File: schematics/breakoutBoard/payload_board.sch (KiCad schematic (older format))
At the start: 5 parts, among them P1 CONN_02X50, P2 CONN_02X50, P3 CONN_02X50, P4 CONN_02X50

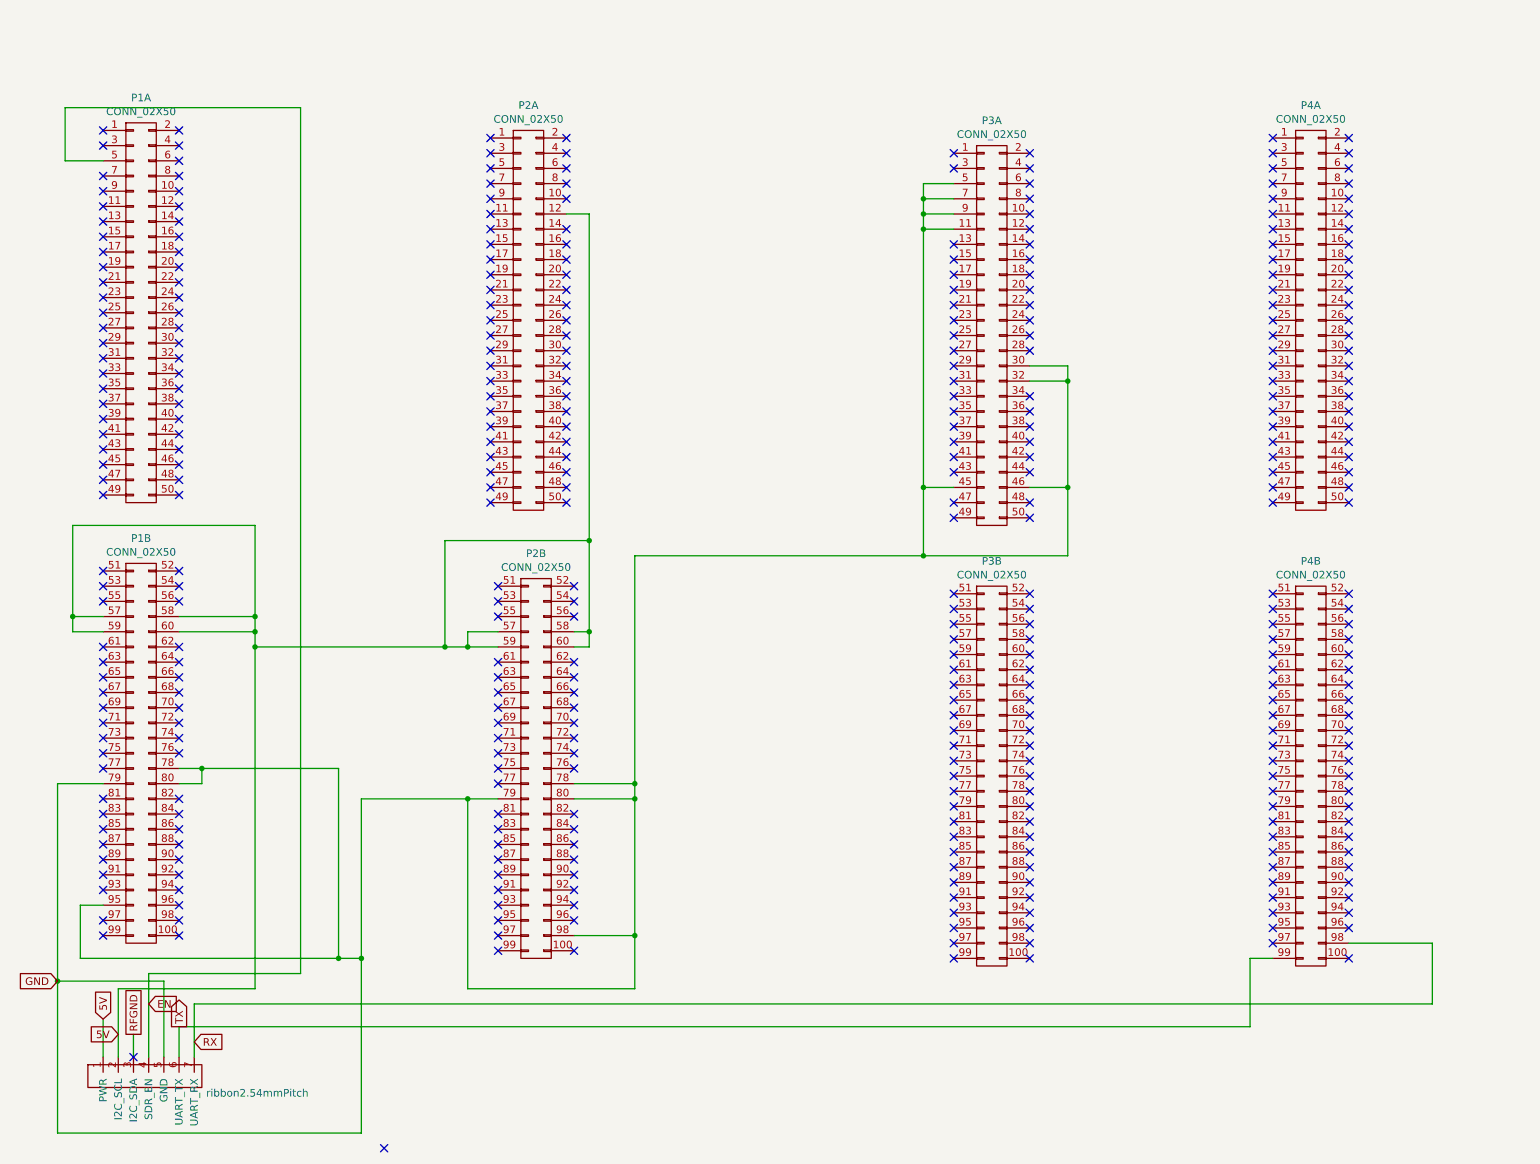
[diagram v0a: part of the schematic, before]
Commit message: Updated schematic
Cleaned up wires and re-did labels. Added additional grounds and verified pwr, TX and RX. Reference to Issues #1, #2, #3 and #5.
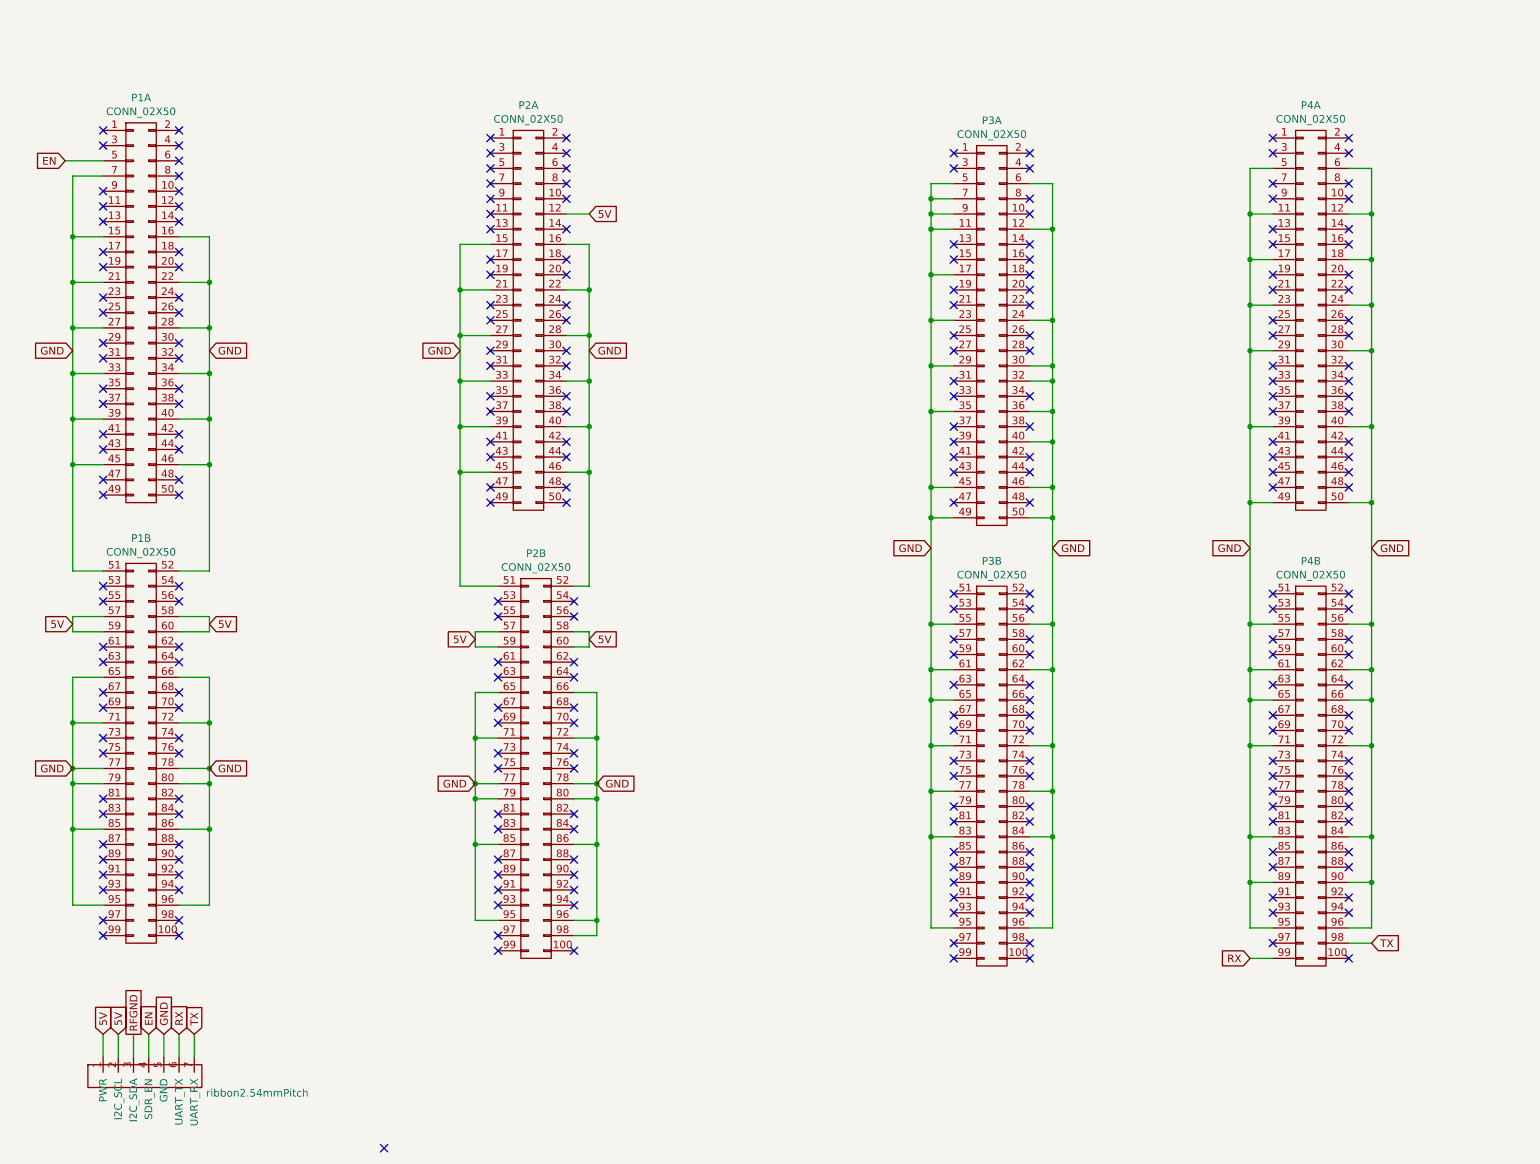
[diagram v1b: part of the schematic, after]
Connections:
- net GND: now also P1.15 (P15), P1.16 (P16), P1.21 (P21), P1.22 (P22), P1.27 (P27), P1.28 (P28), P1.33 (P33), P1.34 (P34), P1.39 (P39), P1.40 (P40), P1.45 (P45), P1.46 (P46), P1.51 (P51), P1.52 (P52), P1.65 (P65), P1.66 (P66), P1.7 (P7), P1.71 (P71), P1.72 (P72), P1.77 (P77), P1.85 (P85), P1.86 (P86), P1.96 (P96), P2.15 (P15), P2.16 (P16), P2.21 (P21), P2.22 (P22), P2.27 (P27), P2.28 (P28), P2.33 (P33), P2.34 (P34), P2.39 (P39), P2.40 (P40), P2.45 (P45), P2.46 (P46), P2.51 (P51), P2.52 (P52), P2.65 (P65), P2.66 (P66), P2.71 (P71), P2.72 (P72), P2.77 (P77), P2.85 (P85), P2.86 (P86), P2.95 (P95), P2.96 (P96), P3.12 (P12), P3.17 (P17), P3.23 (P23), P3.24 (P24), P3.29 (P29), P3.35 (P35), P3.36 (P36), P3.40 (P40), P3.49 (P49), P3.50 (P50), P3.55 (P55), P3.56 (P56), P3.6 (P6), P3.61 (P61), P3.62 (P62), P3.65 (P65), P3.71 (P71), P3.72 (P72), P3.77 (P77), P3.78 (P78), P3.83 (P83), P3.84 (P84), P3.95 (P95), P3.96 (P96), P4.11 (P11), P4.12 (P12), P4.17 (P17), P4.18 (P18), P4.23 (P23), P4.24 (P24), P4.29 (P29), P4.30 (P30), P4.39 (P39), P4.40 (P40), P4.49 (P49), P4.5 (P5), P4.50 (P50), P4.55 (P55), P4.56 (P56), P4.6 (P6), P4.61 (P61), P4.62 (P62), P4.65 (P65), P4.66 (P66), P4.71 (P71), P4.72 (P72), P4.83 (P83), P4.84 (P84), P4.89 (P89), P4.90 (P90), P4.95 (P95), P4.96 (P96)
- net RX: now also P4.99 (P99), e1.6 (UART_TX); no longer P4.98 (P98), e1.7 (UART_RX)
- net TX: now also P4.98 (P98), e1.7 (UART_RX); no longer P4.99 (P99), e1.6 (UART_TX)
- no-connect marks 374 -> 275

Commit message: Move files from main repo
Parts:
- removed e1: ribbon2.54mmPitch, Connector_PinHeader_2.54mm:PinHeader_1x07_P2.54mm_Vertical, symbol payload_board-rescue:ribbon2.54mmPitch
- added H1, H2, H3, H4, H5, H6, H7: MountingHole_Pad, MountingHole:MountingHole_2.2mm_M2_Pad, symbol Mechanical:MountingHole_Pad
- added J1: Conn_01x10, Connector_PinHeader_2.54mm:PinHeader_1x10_P2.54mm_Vertical, symbol Connector_Generic:Conn_01x10
- added SMA1, SMA2: Molex-MMCX-SMD, Mounting_Holes:Molex MMCX SMD 50Ohm, symbol payload_board-rescue:Molex-MMCX-SMD
- P1, P2, P3, P4: footprint breakoutBoard:BERGSTAK_100_PIN1_RIGHT -> 61083-101400LF:FCI_61083-101400LF
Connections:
- net GND: now also J1.10 (Pin_10); no longer P1.15 (P15), P1.16 (P16), P1.21 (P21), P1.22 (P22), P1.27 (P27), P1.28 (P28), P1.33 (P33), P1.34 (P34), P1.39 (P39), P1.40 (P40), P1.45 (P45), P1.46 (P46), P1.51 (P51), P1.52 (P52), P1.65 (P65), P1.66 (P66), P1.7 (P7), P1.71 (P71), P1.72 (P72), P1.77 (P77), P1.78 (P78), P1.79 (P79), P1.80 (P80), P1.85 (P85), P1.86 (P86), P1.95 (P95), P1.96 (P96), P2.15 (P15), P2.16 (P16), P2.21 (P21), P2.22 (P22), P2.27 (P27), P2.28 (P28), P2.33 (P33), P2.34 (P34), P2.39 (P39), P2.40 (P40), P2.45 (P45), P2.46 (P46), P2.51 (P51), P2.52 (P52), P2.65 (P65), P2.66 (P66), P2.71 (P71), P2.72 (P72), P2.77 (P77), P2.85 (P85), P2.86 (P86), P2.95 (P95), P2.96 (P96), P2.98 (P98), P3.12 (P12), P3.17 (P17), P3.23 (P23), P3.24 (P24), P3.29 (P29), P3.35 (P35), P3.36 (P36), P3.40 (P40), P3.45 (P45), P3.46 (P46), P3.49 (P49), P3.50 (P50), P3.55 (P55), P3.56 (P56), P3.6 (P6), P3.61 (P61), P3.62 (P62), P3.65 (P65), P3.71 (P71), P3.72 (P72), P3.77 (P77), P3.78 (P78), P3.83 (P83), P3.84 (P84), P3.95 (P95), P3.96 (P96), P4.11 (P11), P4.12 (P12), P4.17 (P17), P4.18 (P18), P4.23 (P23), P4.24 (P24), P4.29 (P29), P4.30 (P30), P4.39 (P39), P4.40 (P40), P4.49 (P49), P4.5 (P5), P4.50 (P50), P4.55 (P55), P4.56 (P56), P4.6 (P6), P4.61 (P61), P4.62 (P62), P4.65 (P65), P4.66 (P66), P4.71 (P71), P4.72 (P72), P4.83 (P83), P4.84 (P84), P4.89 (P89), P4.90 (P90), P4.95 (P95), P4.96 (P96)
- net SDA1: now reaches P2.13 (P13)
- net SDA1: now also H5.1, J1.7 (Pin_7)
- net SCL1: now reaches P2.14 (P14)
- net SCL1: now also H6.1, J1.8 (Pin_8)
- net SCL0: now reaches P2.17 (P17)
- net SCL0: now also H4.1, J1.6 (Pin_6)
- net SDA0: now reaches P2.19 (P19)
- net SDA0: now also H3.1, J1.5 (Pin_5)
- net ENABLE: now reaches P2.5 (P5)
- net ENABLE: now also H7.1, J1.9 (Pin_9)
- net UART_TX: now reaches P4.14 (P14)
- net UART_TX: now also H2.1, J1.4 (Pin_4)
- net UART_RX: now reaches P4.16 (P16)
- net UART_RX: now also H1.1, J1.3 (Pin_3)
- net 5V renamed 5v
- net 5v: now also J1.1 (Pin_1)
- net EN: no longer names the net of P1.5 (P5)
- net RX: no longer names the net of P4.99 (P99)
- net TX: no longer names the net of P4.98 (P98)
- new net: SMA1.1 (RF_DATA), SMA2.1 (RF_DATA)
- new net 3.3v: J1.2 (Pin_2), P1.78 (P78), P1.79 (P79), P1.80 (P80), P2.98 (P98), P3.45 (P45), P3.46 (P46)
- no-connect marks 275 -> 0
